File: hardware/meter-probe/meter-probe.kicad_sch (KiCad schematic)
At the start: 17 parts, among them J1 Main Board, Q1 BSS138, SW1 Sensor Button, U1 RT9193, U2 TCS3472, U3 P82B96

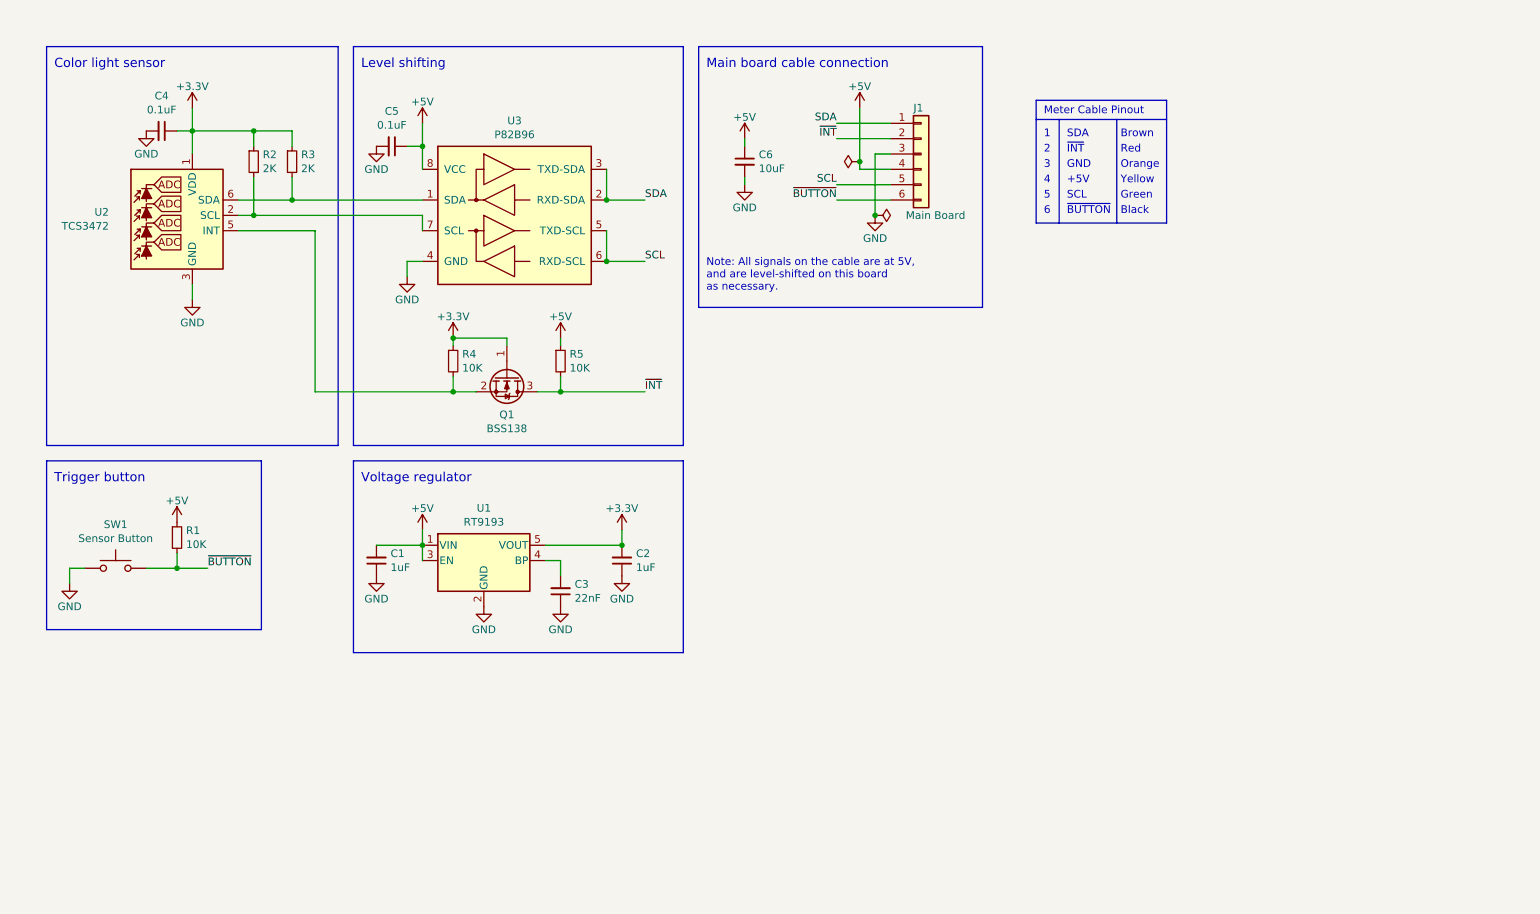
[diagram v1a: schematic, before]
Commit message: First pass at updating meter probe schematic
At this stage, the goal is not to change the sensor, but to update
everything else that is unlikely to meaningfully differ if the sensor is
changed.
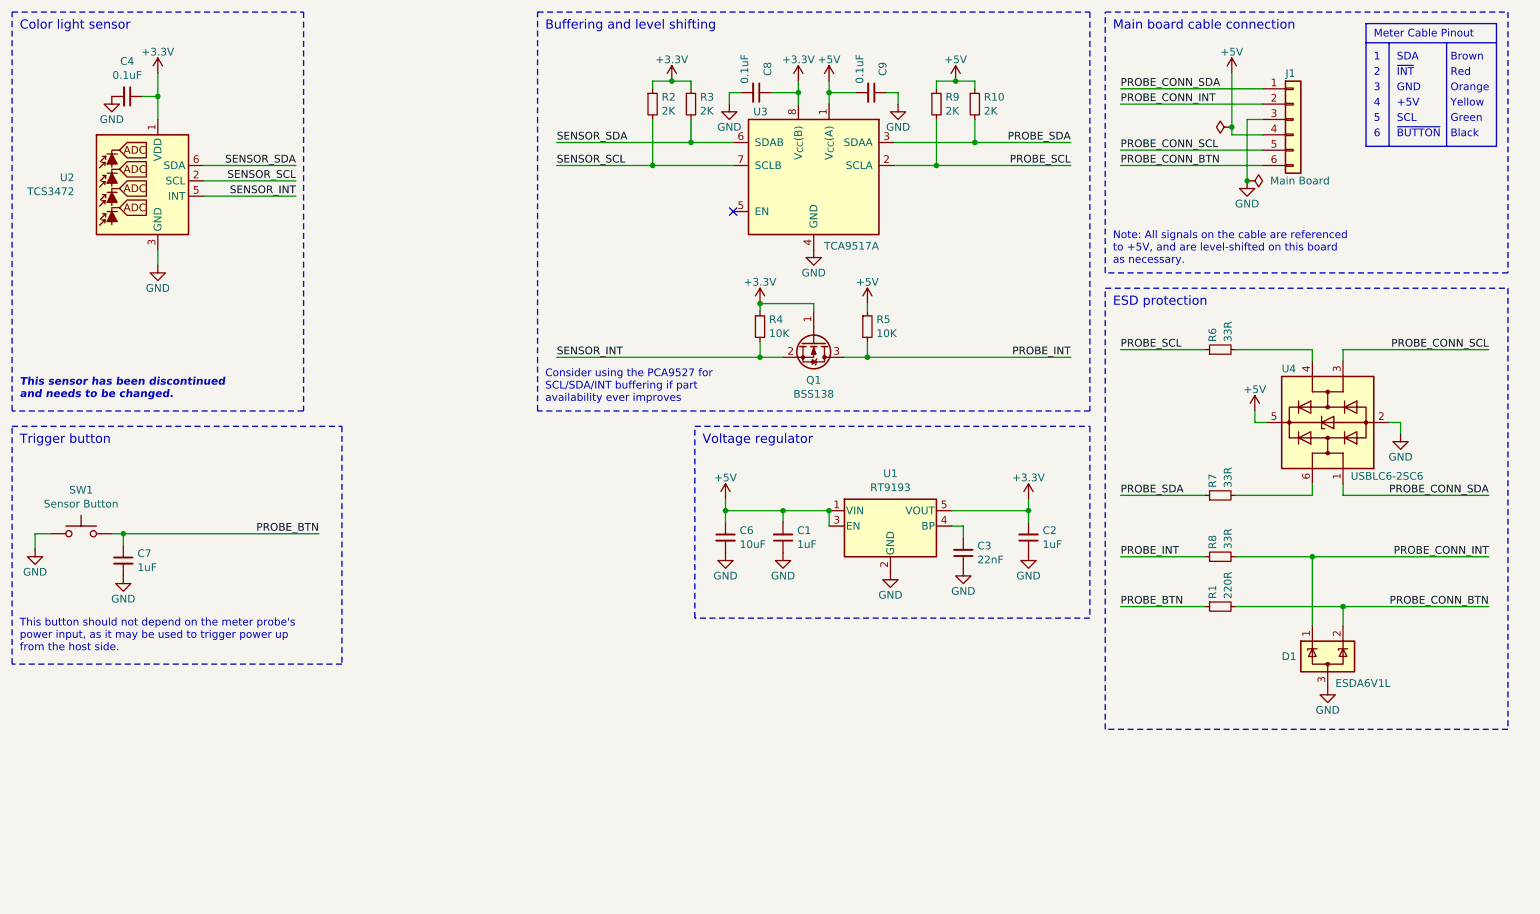
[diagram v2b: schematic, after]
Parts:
- removed C5: 0.1uF, Capacitor_SMD:C_0603_1608Metric, symbol Device:C_Small
- removed U3: P82B96, Package_SO:SOIC-8_3.9x4.9mm_P1.27mm, symbol Interface_Expansion:P82B96
- added C7: 1uF, Capacitor_SMD:C_0603_1608Metric, symbol Device:C_Small
- added C8, C9: 0.1uF, Capacitor_SMD:C_0603_1608Metric, symbol Device:C_Small
- added D1: ESDA6V1L, lib_fp:SOT23-3L, symbol Project:ESDA6V1L
- added R10, R9: 2K, Resistor_SMD:R_0603_1608Metric, symbol Device:R_Small
- added R6, R7, R8: 33R, Resistor_SMD:R_0603_1608Metric, symbol Device:R_Small
- added U3: TCA9517A, Package_SO:VSSOP-8_3.0x3.0mm_P0.65mm, symbol Project:TCA9517A
- added U4: USBLC6-2SC6, Package_TO_SOT_SMD:SOT-23-6, symbol Power_Protection:USBLC6-2SC6
- R1: value 10K -> 220R; Manufacturer Vishay Dale -> YAGEO; Manufacturer PN CRCW060310K0JNEA -> RC0603JR-07220RL; Supplier PN 541-10KGCT-ND -> 311-220GRCT-ND
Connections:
- net +3.3V: now also C8.1, U3.8 (V_{CC}(B))
- net +5V: now also C9.2, R10.1, R9.1, U3.1 (V_{CC}(A)), U4.5 (VBUS); no longer R1.1
- net GND: now also C7.2, C8.2, C9.1, D1.3 (A), U3.4 (GND), U4.2 (GND)
- net SENSOR_SCL: now reaches R2.2, U2.2 (SCL)
- net SENSOR_SCL: now also U3.7 (SCLB)
- net SENSOR_INT: now reaches Q1.2 (S), R4.2, U2.5 (INT)
- net SENSOR_SDA: now reaches R3.2, U2.6 (SDA)
- net SENSOR_SDA: now also U3.6 (SDAB)
- net SCL renamed PROBE_CONN_SCL
- net PROBE_CONN_SCL: now also U4.3 (I/O2)
- net SDA renamed PROBE_CONN_SDA
- net PROBE_CONN_SDA: now also U4.1 (I/O1)
- net ~{BUTTON} renamed PROBE_CONN_BTN
- net PROBE_CONN_BTN: now also D1.2 (K); no longer SW1.2
- net ~{INT} renamed PROBE_INT
- net PROBE_INT: now also R8.1; no longer J1.2 (Pin_2)
- new net: R6.2, U4.4 (I/O2)
- new net: R7.2, U4.6 (I/O1)
- new net PROBE_BTN: C7.1, R1.1, SW1.2
- new net PROBE_CONN_INT: D1.1 (K), J1.2 (Pin_2), R8.2
- new net PROBE_SCL: R6.1, R9.2, U3.2 (SCLA)
- new net PROBE_SDA: R10.2, R7.1, U3.3 (SDAA)
- no-connect marks 0 -> 1
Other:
- note added: "Buffering and level shifting"
- note added: "Consider using the PCA9527 for SCL/SDA/INT buffering if part availability ever improves"
- note added: "ESD protection"
- note added: "Note: All signals on the cable are referenced to +5V, and are level-shifted on this board as necessary."
- note added: "This button should not depend on the meter probe's power input, as it may be used to trigger power up from the host side."
- note added: "This sensor has been discontinued and needs to be changed."
- note removed: "Level shifting"
- note removed: "Note: All signals on the cable are at 5V, and are level-shifted on this board as necessary."
- moved on the sheet: C1, C2, C3, C4, C6, J1, Q1, R2, R3, R4, R5, SW1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

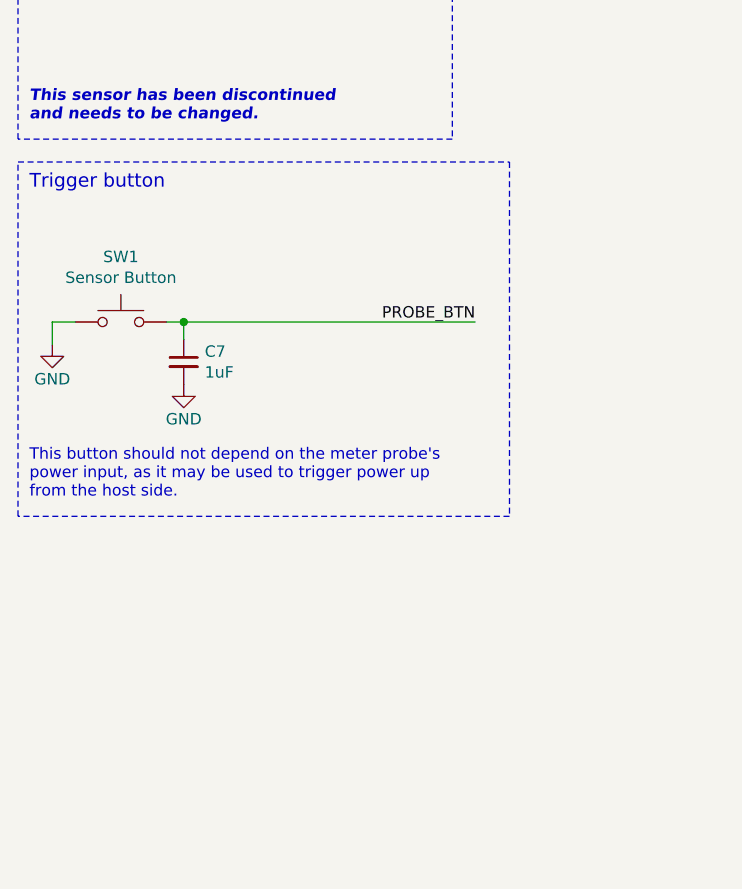
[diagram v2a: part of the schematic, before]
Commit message: Added I2C EEPROM to schematic
This will be used for meter probe identification and calibration data
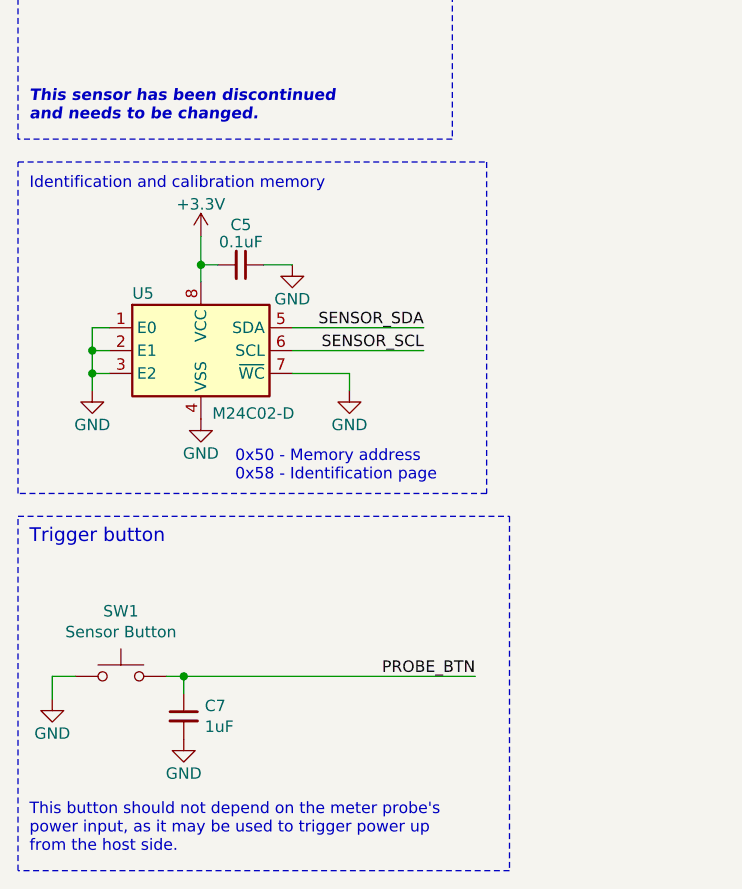
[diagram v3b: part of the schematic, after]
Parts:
- added C5: 0.1uF, Capacitor_SMD:C_0603_1608Metric, symbol Device:C_Small
- added U5: M24C02-D, Package_SO:TSSOP-8_4.4x3mm_P0.65mm, symbol Memory_EEPROM:M24C02-RDW
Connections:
- net +3.3V: now also C5.2, U5.8 (VCC)
- net GND: now also C5.1, U5.1 (E0), U5.2 (E1), U5.3 (E2), U5.4 (VSS), U5.7 (~{WC})
- net SENSOR_SCL: now also U5.6 (SCL)
- net SENSOR_SDA: now also U5.5 (SDA)
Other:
- note added: "0x50 - Memory address 0x58 - Identification page"
- note added: "Identification and calibration memory"
- moved on the sheet: C7, SW1

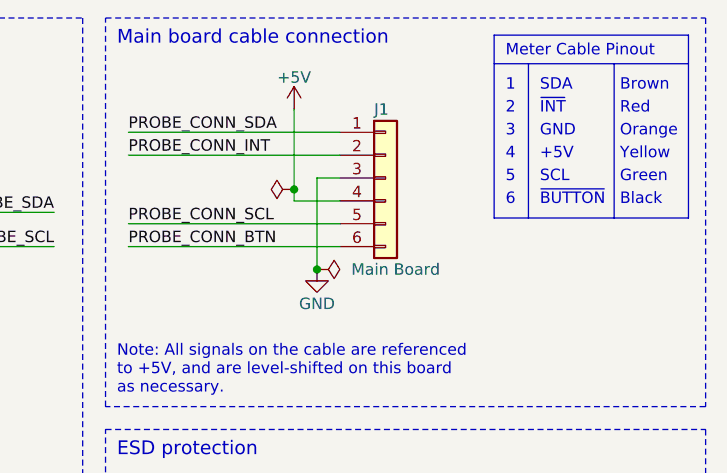
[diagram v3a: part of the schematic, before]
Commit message: Add IDC connector to schematic
This replaces a single 6-pin part with two 3-pin parts
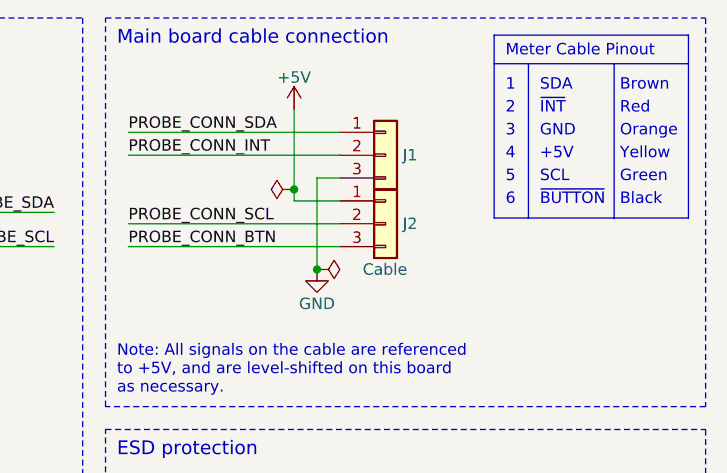
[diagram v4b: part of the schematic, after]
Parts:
- removed J1: Main Board, lib_fp:SolderWire-0.1sqmm_1x06_Cable, symbol Connector_Generic:Conn_01x06
- added J1, J2: Cable, lib_fp:AVX_IDC-009175-003-001, symbol Connector_Generic:Conn_01x03
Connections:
- net +5V: now also J2.1 (Pin_1)
- net GND: now also J1.3 (Pin_3)
- net PROBE_CONN_BTN: now also J2.3 (Pin_3)
- net PROBE_CONN_INT: now also J1.2 (Pin_2)
- net PROBE_CONN_SCL: now also J2.2 (Pin_2)
- net PROBE_CONN_SDA: now also J1.1 (Pin_1)
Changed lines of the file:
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@@
-    )
-  )
-  (symbol (lib_id "Connector_Generic:Conn_01x06") (at 227.965 33.655 0) (unit 1)
-    (in_bom yes) (on_board yes) (dnp no)
-    (property "Reference" "J1" (at 226.695 26.035 0)
-      (effects (font (size 1.27 1.27)) (justify left))
-    )
-    (property "Value" "Main Board" (at 224.155 43.815 0)
-      (effects (font (size 1.27 1.27)) (justify left))
-    )
-    (property "Footprint" "lib_fp:SolderWire-0.1sqmm_1x06_Cable" (at 227.965 33.655 0)
-      (effects (font (size 1.27 1.27)) hide)
-    )
-    (property "Datasheet" "~" (at 227.965 33.655 0)
-      (effects (font (size 1.27 1.27)) hide)
-    )
-    (property "Description" "WIRE-TO-BOARD" (at 227.965 33.655 0)
-      (effects (font (size 1.27 1.27)) hide)
-    )
-    (property "Manufacturer" "" (at 227.965 33.655 0)
-      (effects (font (size 1.27 1.27)) hide)
-    )
-    (property "Manufacturer PN" "" (at 227.965 33.655 0)
-      (effects (font (size 1.27 1.27)) hide)
-    )
-    (property "Supplier" "" (at 227.965 33.655 0)
-      (effects (font (size 1.27 1.27)) hide)
-    )
-    (property "Supplier PN" "" (at 227.965 33.655 0)
-      (effects (font (size 1.27 1.27)) hide)
-    )
-    (pin "1")
-    (pin "2")
-    (pin "3")
-    (pin "4")
-    (pin "5")
-    (pin "6")
-    (instances
-      (project "meter-probe"
-        (path "/1f1005f7-3f58-4453-9bfa-bdc1c0b6f7ed"
-          (reference "J1") (unit 1)
-        )
-      )
     )
   )
@@
     )
   )
+  (symbol (lib_id "Connector_Generic:Conn_01x03") (at 227.965 38.735 0) (unit 1)
+    (in_bom yes) (on_board yes) (dnp no)
+    (property "Reference" "J2" (at 229.87 38.735 0)
+      (effects (font (size 1.27 1.27)) (justify left))
+    )
+    (property "Value" "Cable" (at 225.425 43.815 0)
+      (effects (font (size 1.27 1.27)) (justify left))
+    )
+    (property "Footprint" "lib_fp:AVX_IDC-009175-003-001" (at 227.965 38.735 0)
+      (effects (font (size 1.27 1.27)) hide)
+    )
+    (property "Datasheet" "https://datasheets.kyocera-avx.com/Standard_00-9175.pdf" (at 227.965 38.735 0)
+      (effects (font (size 1.27 1.27)) hide)
+    )
+    (property "Description" "3-WAY WIRE TO BOARD 28 AWG" (at 227.965 38.735 0)
+      (effects (font (size 1.27 1.27)) hide)
+    )
+    (property "Manufacturer" "KYOCERA AVX" (at 227.965 38.735 0)
+      (effects (font (size 1.27 1.27)) hide)
+    )
+    (property "Manufacturer PN" "009175003001006" (at 227.965 38.735 0)
+      (effects (font (size 1.27 1.27)) hide)
+    )
+    (property "Supplier" "Mouser" (at 227.965 38.735 0)
+      (effects (font (size 1.27 1.27)) hide)
+    )
+    (property "Supplier PN" "581-009175003001006" (at 227.965 38.735 0)
+      (effects (font (size 1.27 1.27)) hide)
+    )
+    (pin "1")
+    (pin "2")
+    (pin "3")
+    (instances
+      (project "meter-probe"
+        (path "/1f1005f7-3f58-4453-9bfa-bdc1c0b6f7ed"
+          (reference "J2") (unit 1)
+        )
+      )
+    )
+  )
   (symbol (lib_id "Device:R_Small") (at 215.9 95.885 90) (unit 1)
     (in_bom yes) (on_board yes) (dnp no)
@@
         )
       )
+    )
+  )
+  (symbol (lib_id "Connector_Generic:Conn_01x03") (at 227.965 31.115 0) (unit 1)
+    (in_bom yes) (on_board yes) (dnp no)
+    (property "Reference" "J1" (at 229.87 31.115 0)
+      (effects (font (size 1.27 1.27)) (justify left))
+    )
+    (property "Value" "Cable" (at 225.425 26.035 0)
+      (effects (font (size 1.27 1.27)) (justify left) hide)
+    )
+    (property "Footprint" "lib_fp:AVX_IDC-009175-003-001" (at 227.965 31.115 0)
+      (effects (font (size 1.27 1.27)) hide)
+    )
+    (property "Datasheet" "https://datasheets.kyocera-avx.com/Standard_00-9175.pdf" (at 227.965 31.115 0)
+      (effects (font (size 1.27 1.27)) hide)
+    )
+    (property "Description" "3-WAY WIRE TO BOARD 28 AWG" (at 227.965 31.115 0)
+      (effects (font (size 1.27 1.27)) hide)
+    )
+    (property "Manufacturer" "KYOCERA AVX" (at 227.965 31.115 0)
+      (effects (font (size 1.27 1.27)) hide)
+    )
+    (property "Manufacturer PN" "009175003001006" (at 227.965 31.115 0)
+      (effects (font (size 1.27 1.27)) hide)
+    )
+    (property "Supplier" "Mouser" (at 227.965 31.115 0)
+      (effects (font (size 1.27 1.27)) hide)
+    )
+    (property "Supplier PN" "581-009175003001006" (at 227.965 31.115 0)
+      (effects (font (size 1.27 1.27)) hide)
+    )
+    (pin "1")
+    (pin "2")
+    (pin "3")
+    (instances
+      (project "meter-probe"
+        (path "/1f1005f7-3f58-4453-9bfa-bdc1c0b6f7ed"
+          (reference "J1") (unit 1)
+        )
+      )
